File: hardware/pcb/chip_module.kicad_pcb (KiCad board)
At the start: 6 copper layers, 85 x 50 mm, 48 parts, among them J1 Samtec LSHM-130, Q1 AO3401A, Q10 AO3400A, Q11 AO3400A, Q12 AO3400A, Q13 AO3400A, Q14 AO3400A, Q15 AO3400A, Q16 AO3400A, Q2 AO3401A, Q3 AO3401A, Q4 AO3401A, Q5 AO3401A, Q6 AO3401A, Q7 AO3401A, Q8 AO3401A, Q9 AO3400A, U1 ADG732BCPZ, U2 ADG732BCPZ, U3 ADA4530-1, U4 74LVC1G04, U5 QSSC_Chip, U6 74HCT240, U7 74HCT240

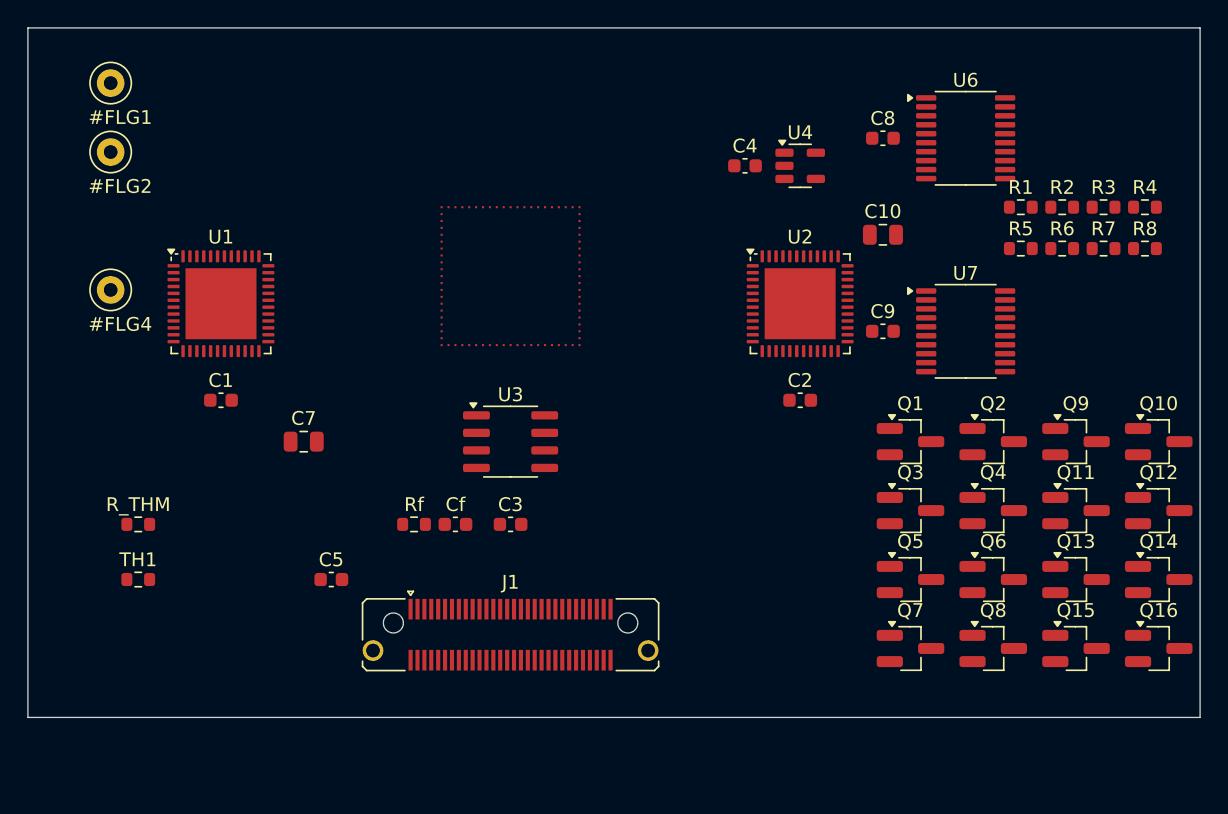
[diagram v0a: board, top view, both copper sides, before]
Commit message: pcb: fix router keepout bugs -> both boards DRC-clean (0/0/0)
The headless line router had three keepout bugs that let a via or track
claim a cell another net already owned, producing DRC shorts on the
production-hardened (denser) board:

1. Centre-only via check. _via_candidates / _bga_edge_via_candidates /
   _via_point_clear only tested the via's centre cell per layer, but
   _add_via then marked a full r3 (0.6 mm) block on all four signal
   layers. A neighbour net's track 0.1-0.6 mm off-centre was invisible,
   so the via was placed and shorted it (CONF_DONE via vs CONF_INIT
   track on In4.Cu; TIA_ADC via vs VREFP track on B.Cu). Fixed with a
   _via_footprint_free helper that checks the full r3 footprint on all
   four signal layers before accepting any via-up.

2. multi_vip (BGA via-in-pad). The per-net vip_net "allowed" override
   seeded each ball's r2 mark on In3/In4/B.Cu. Adjacent 0.5 mm-pitch
   balls' r2 marks overlap by 0.3 mm, and the override let a net's own
   track/via-up enter that overlap -> ~0.10 mm clearance to the
   neighbour VIP. The multi_keepout fix (for pads) did not cover VIPs.
   Fixed by building a multi_vip set (cells in >=2 nets' VIP marks) and
   subtracting it from every net's vip_net, mirroring multi_keepout.

3. multi_keepout (pads) -- already applied last session (mw_gate->GND
   short on the D10 ESD diode). Kept; documented alongside multi_vip.

Result: both boards regenerate + route DRC-clean headlessly:
  qssc:        14/71 non-plane nets, 217 tracks, 95 vias, 0 DRC violations
  chip_module: 11/133 nets, 140 tracks, 47 vias, 0 DRC violations
ERC: 0 errors on both schematics (warnings only).

The router is now provably no-short-by-construction, but the correct
keepouts are conservative (a THROUGH via-up needs its full 0.6 mm
footprint clear on all four signal layers, which the dense 0.5 mm BGA
escape rarely affords), so completeness dropped from a buggy 37 (centre-
only check placed shorting vias) to a correct 14. The headles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
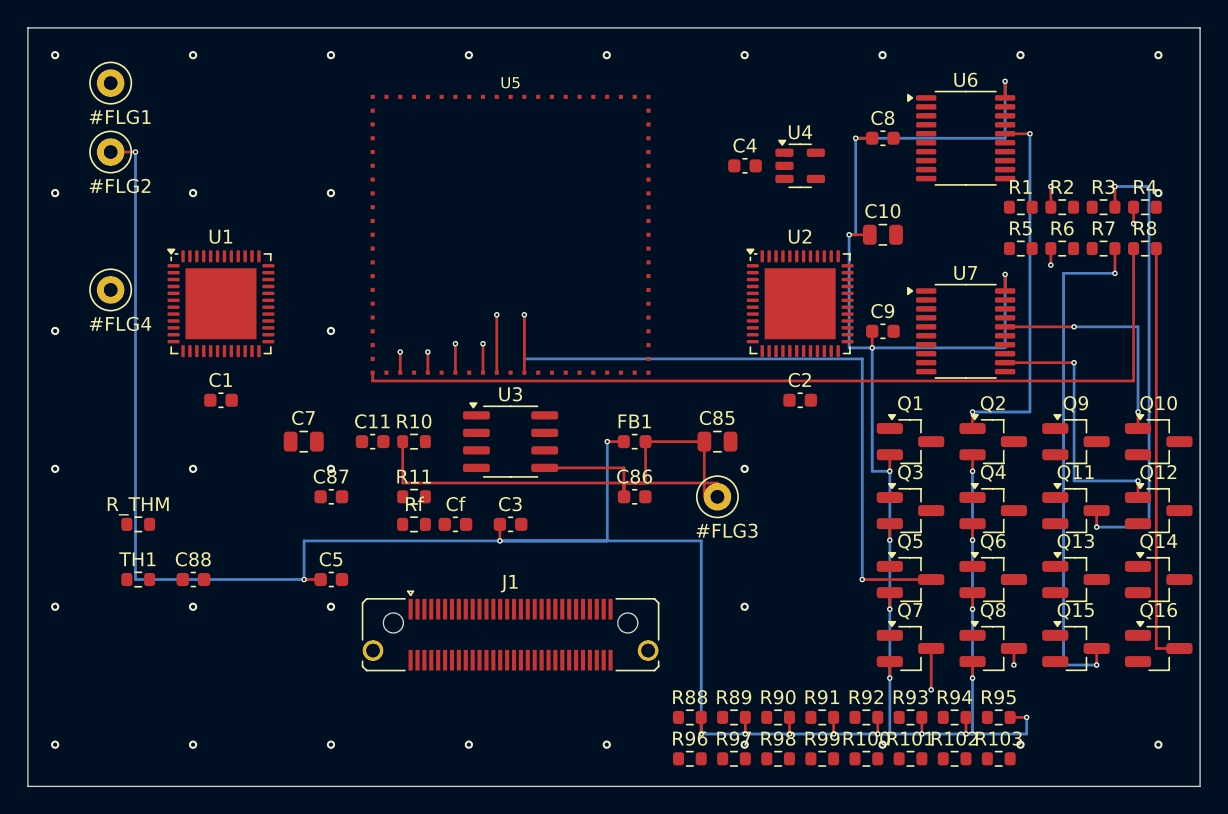
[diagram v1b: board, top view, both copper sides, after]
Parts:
- added #FLG3: PWR_FLAG, TestPoint_Loop_D1.80mm_Drill1.0mm_Beaded, F.Cu at (50.0, 34.0)
- added C11: 100nF, C_0603_1608Metric, F.Cu at (25.0, 30.0)
- added C85: 10uF, C_0805_2012Metric, F.Cu at (50.0, 30.0)
- added C86: 100nF, C_0603_1608Metric, F.Cu at (44.0, 34.0)
- added C87: 1uF, C_0603_1608Metric, F.Cu at (22.0, 34.0)
- added C88: 100nF, C_0603_1608Metric, F.Cu at (12.0, 40.0)
- added FB1: 600Ω@100MHz, L_0603_1608Metric, F.Cu at (44.0, 30.0)
- added R10: 10k, R_0603_1608Metric, F.Cu at (28.0, 30.0)
- added R100: 100k, R_0603_1608Metric, F.Cu at (60.8, 53.0)
- added R101: 100k, R_0603_1608Metric, F.Cu at (64.0, 53.0)
- added R102: 100k, R_0603_1608Metric, F.Cu at (67.2, 53.0)
- added R103: 100k, R_0603_1608Metric, F.Cu at (70.4, 53.0)
- added R11: 10k, R_0603_1608Metric, F.Cu at (28.0, 34.0)
- added R88: 100k, R_0603_1608Metric, F.Cu at (48.0, 50.0)
- added R89: 100k, R_0603_1608Metric, F.Cu at (51.2, 50.0)
- added R90: 100k, R_0603_1608Metric, F.Cu at (54.4, 50.0)
- added R91: 100k, R_0603_1608Metric, F.Cu at (57.6, 50.0)
- added R92: 100k, R_0603_1608Metric, F.Cu at (60.8, 50.0)
- added R93: 100k, R_0603_1608Metric, F.Cu at (64.0, 50.0)
- added R94: 100k, R_0603_1608Metric, F.Cu at (67.2, 50.0)
- added R95: 100k, R_0603_1608Metric, F.Cu at (70.4, 50.0)
- added R96: 100k, R_0603_1608Metric, F.Cu at (48.0, 53.0)
- added R97: 100k, R_0603_1608Metric, F.Cu at (51.2, 53.0)
- added R98: 100k, R_0603_1608Metric, F.Cu at (54.4, 53.0)
- added R99: 100k, R_0603_1608Metric, F.Cu at (57.6, 53.0)
- moved U5 3.00 mm to (35.0, 15.0)
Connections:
- C3 pad 1: +3V3 -> +5V
- U3 pad 2: (no net) -> TIA_REF
- U3 pad 5: +3V3 -> +5V_TIA
- U3 pad 7: (no net) -> TIA_REF
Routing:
- net +5V: track 0.00 -> 256.5 mm, vias 0 -> 25
- net emitter_anode6: track 0.00 -> 69.5 mm, vias 0 -> 2
- net emitter_anode7: track 0.00 -> 65.9 mm, vias 0 -> 2
- net emitter_cathode7: track 0.00 -> 65.4 mm
- net emitter_cathode3: track 0.00 -> 63.2 mm, vias 0 -> 2
- net emitter_cathode1: track 0.00 -> 58.2 mm, vias 0 -> 2
- net emitter_cathode5: track 0.00 -> 57.8 mm, vias 0 -> 2
- net emitter_anode4: track 0.00 -> 52.9 mm, vias 0 -> 2
- net +5V_TIA: track 0.00 -> 49.4 mm
- net col_sink6: track 0.00 -> 37.5 mm, vias 0 -> 2
- net col_sink2: track 0.00 -> 33.7 mm, vias 0 -> 2
- net col_sink7: track 0.00 -> 30.7 mm
- net row_gate1: track 0.00 -> 27.3 mm, vias 0 -> 2
- net col_gate3: track 0.00 -> 19.4 mm, vias 0 -> 2
- net col_gate1: track 0.00 -> 17.0 mm, vias 0 -> 2
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- added copper zone on In2.Cu, net +3V3
- added copper zone on In1.Cu, net GND
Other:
- board size 85 x 50 mm -> 85 x 55 mm

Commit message: pcb: tie every IC power/ground pad to its plane (rect pad model + F.Cu tie traces)
The plane router previously placed an offset via near each surface GND/+3V3
SMD pad but emitted no pad-to-via trace, so the pad floated off the plane —
hidden by the board's `unconnected_items: ignore`. The offset-via "0 untied"
metric was misleading. This makes the connection real and verifies it per-IC.

route_qssc_pcb.py:
  - Rectangle-accurate pad obstacle model (_pad_obstacle now returns the pad's
    true half-extents from GetSize, not a half-diagonal circle). A 0.25x0.88 mm
    QFN lead is 0.125 mm off its narrow side; the old 0.46 mm "radius" circle
    falsely blocked a via that clears the narrow side by 0.45 mm. With the
    rectangle, dense 0.5 mm-pitch fanout places.
  - 0.16 mm copper gap (just over the 0.15 mm Power netclass rule), down from
    a 0.5 mm via-vs-circle min_clear sized for a 0.3 mm via, not a 0.4 mm trace.
  - F.Cu tie trace (0.4 mm) pad-centre -> via-centre for every offset rail via,
    so the surface pad actually reaches its inner plane. Via-in-pad kept for
    the large QFN/LFCSP centre exposed-pads (U3, U1/U2 module MUX EPs).
  - Layer-aware trace check: the F.Cu tie trace is checked against F.Cu signal
    tracks only (sig_segs_fcu), never In3/In4/B.Cu tracks it cannot reach; the
    through via is still checked against all-layer tracks.
  - Shared tie_segs list threaded through both rail passes so a +3V3 trace/via
    keeps copper gap to a GND trace/via the first pass placed (parallel 0.5 mm
    fanouts would otherwise leave a 0.1 mm gap < the 0.15 mm rule).
  - Idempotency fix: _signal_obstacles now skips +3V3 (as well as GND). Both are
    this router's domain (route_signals never routes them), so a prior run's
    +3V3 tie traces/vias captured before _clear_routed were ghost obstacles
    that blocked the next +3V3 pass, oscillating the via count 0/40/0/40.

route_signals.py: Phase D daisy-chain fallback (prior session, now committed) —
  a strag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
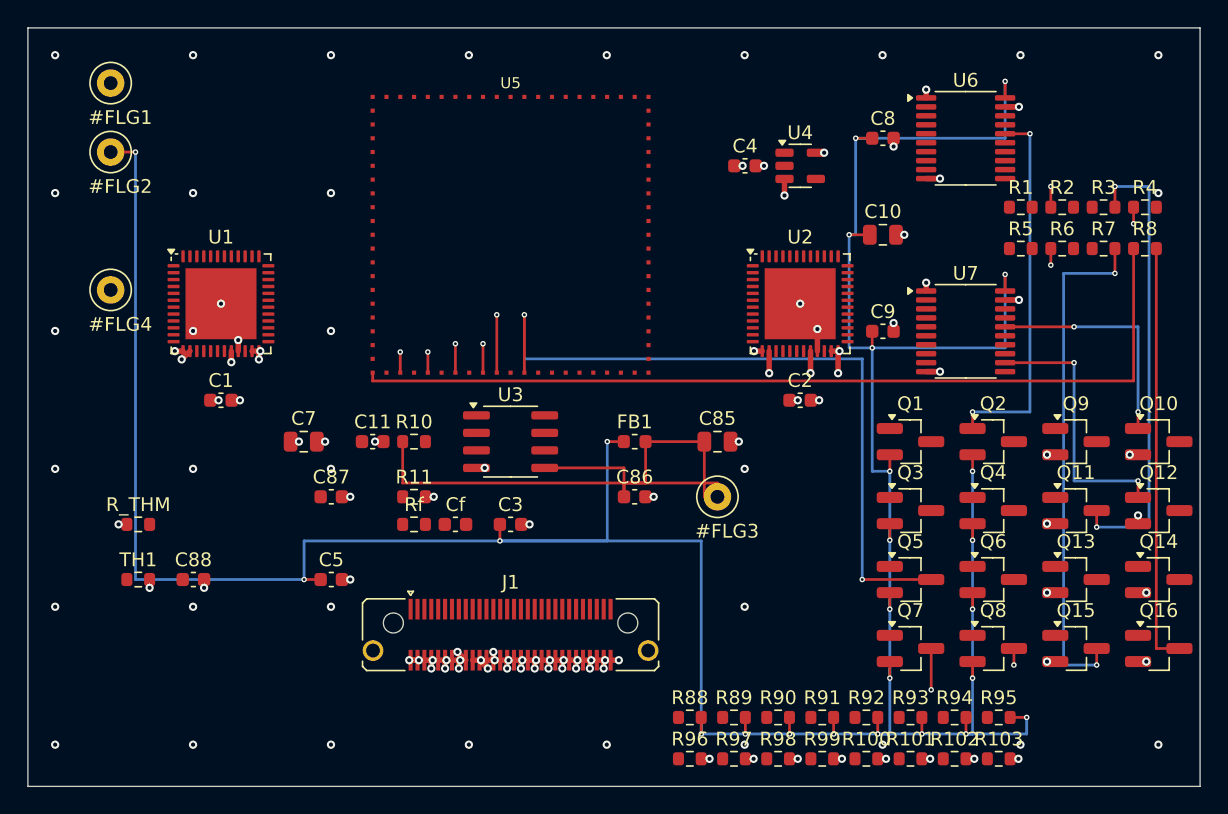
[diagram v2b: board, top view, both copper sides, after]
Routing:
- net GND: track 0.00 -> 52.9 mm, vias 32 -> 113
- net +3V3: track 0.00 -> 7.25 mm, vias 0 -> 10
